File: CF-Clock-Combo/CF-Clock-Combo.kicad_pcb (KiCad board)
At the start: 2 copper layers, 99.9 x 99.9 mm, 19 parts, among them J1 IDE_CONNECTOR, J2 CF Adapter Power, J3 Jumpers, J4 Bus_ISA_8bit, U1 BIOS FLASH, U2 74HCT245, U3 GAL22V10, U4 DS1315, Y1 32.768 KHz

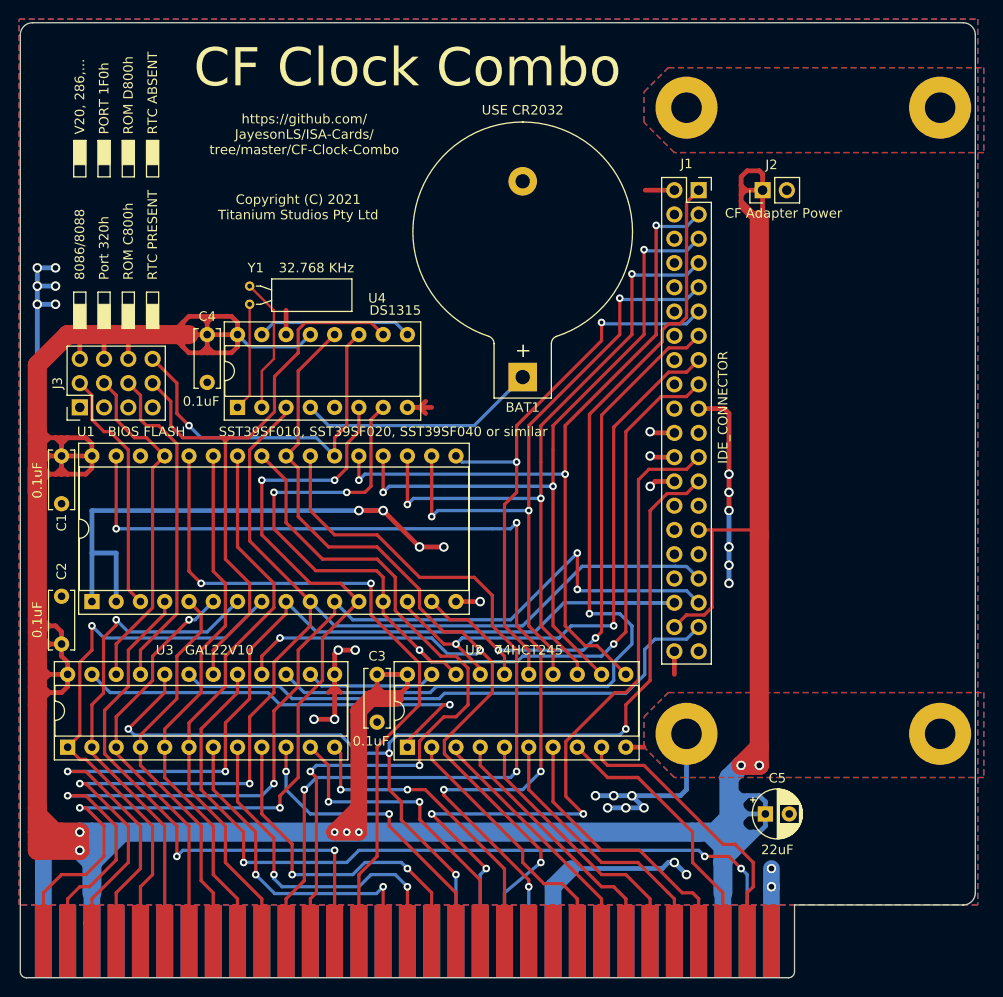
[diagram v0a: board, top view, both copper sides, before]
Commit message: Fix location of CF adapter power for all boards that use it. Also the mounting holes in the schematic for the same boards. Finishing touches to Tandy 1000 Essentials.
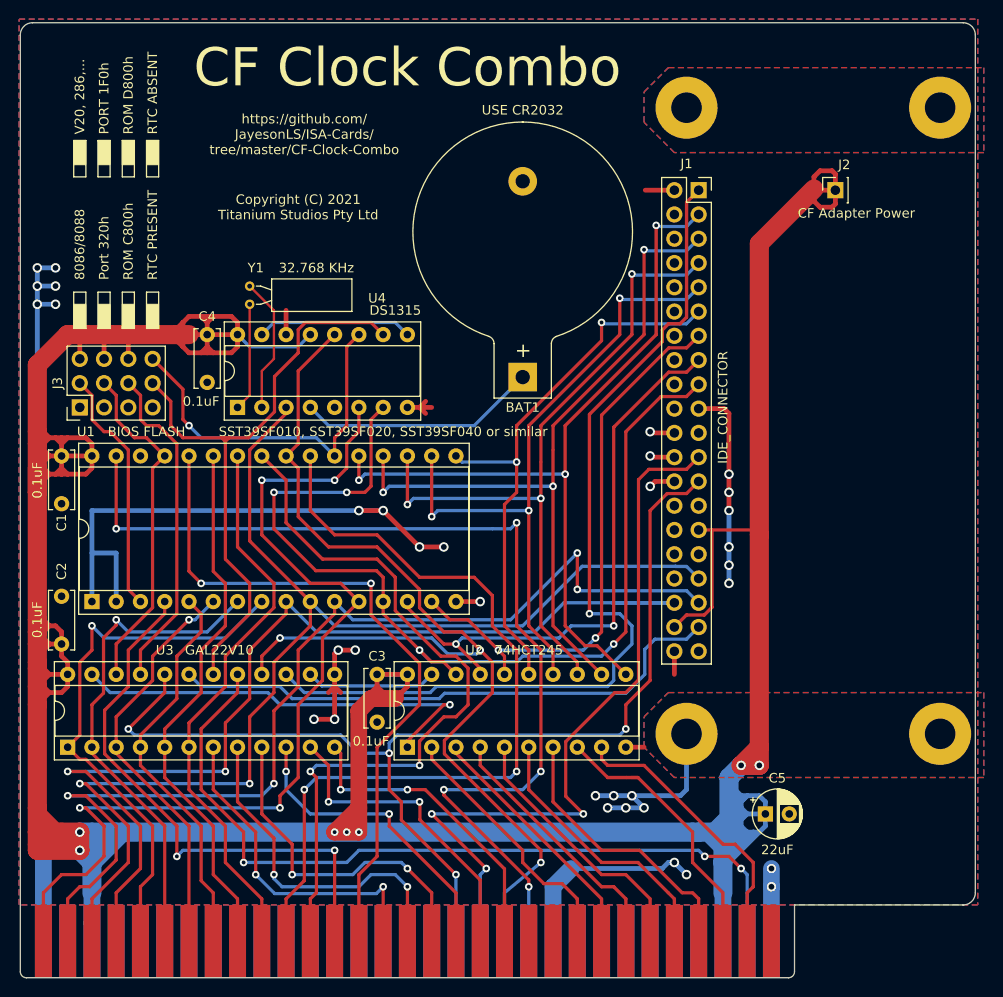
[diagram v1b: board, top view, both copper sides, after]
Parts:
- H1: renamed from MH1; value MH -> MountingHole_Pad
- H2: renamed from MH2; value MH -> MountingHole_Pad
- H3: renamed from MH3; value MH -> MountingHole_Pad
- H4: renamed from MH4; value MH -> MountingHole_Pad
- J2: footprint Connector_PinHeader_2.54mm:PinHeader_1x02_P2.54mm_Vertical -> Connector_PinSocket_2.54mm:PinSocket_1x01_P2.54mm_Vertical
- moved J2 7.62 mm to (182.0, 59.8)
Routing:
- net VCC: track 519.5 -> 520.5 mm
